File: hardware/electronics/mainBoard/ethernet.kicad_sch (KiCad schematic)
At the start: 29 parts, among them U4 LAN8742AI, U5 MRJ-5381-01

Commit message: fixed nets
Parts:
- removed C57: 1uF, symbol lib_sch:C
- removed C58, C59, C60: 100nF, symbol lib_sch:C
- removed C61: 10uF, symbol lib_sch:C
- removed C63: 100nF, symbol lib_sch:C_horizontal
- removed R31, R39: 33R, symbol lib_sch:R_horizontal
- removed R32: 10K, symbol lib_sch:R_horizontal
- removed R33, R34, R35, R36, R37, R47: 10K, symbol lib_sch:R
- removed R42, R43: 40R9, symbol lib_sch:R
- removed R45: 270R, symbol lib_sch:R
- added C47: 10uF, symbol lib_sch:C
- added C48, C49, C53: 100nF, symbol lib_sch:C
- added C50: 100nF, symbol lib_sch:C_horizontal
- added C52: 1uF, symbol lib_sch:C
- added R25, R26, R27: 41K2, symbol lib_sch:R
- added R28, R29, R30, R31, R32, R40: 10K, symbol lib_sch:R
- added R34, R36: 33R, symbol lib_sch:R_horizontal
- added R35: 10K, symbol lib_sch:R_horizontal
- C51: renamed from C56; DKPN (none) -> 478-12726-1-ND; MPN (none) -> 06035C471K4T4A; Manufacturer (none) -> KYOCERA AVX; Package PKG -> 0603; Tolerance TOL -> 10%; Voltage Rating VOLTAGE -> 50V
- L3: Current Rating IMAX -> 350mA; DC Resistance DCR -> 500mR; DKPN (none) -> 283-MFBA3V1608K-601-RCT-ND; MPN (none) -> MFBA3V1608K-601-R; Manufacturer (none) -> Eaton - Electronics Division; Package PKG -> 0603
- R24: renamed from R40; value 40R9 -> 41K2; DKPN (none) -> 541-41.2LCT-ND; MPN (none) -> CRCW040241R2FKED; Manufacturer (none) -> Vishay Dale; Package PKG -> 0402; Power Rating PWR -> 62m5W; Tolerance TOL -> 1%
- R33: renamed from R30; DKPN (none) -> 541-33.0LCT-ND; MPN (none) -> CRCW040233R0FKED; Manufacturer (none) -> Vishay Dale; Package PKG -> 0402; Power Rating PWR -> 62m5W; Tolerance TOL -> 1%
- R37: renamed from R44; DKPN (none) -> 541-12.1KLCT-ND; MPN (none) -> CRCW040212K1FKED; Manufacturer (none) -> Vishay Dale; Package PKG -> 0402; Power Rating PWR -> 62m5W; Tolerance TOL -> 1%
- R38: DKPN (none) -> 541-33.0LCT-ND; MPN (none) -> CRCW040233R0FKED; Manufacturer (none) -> Vishay Dale; Package PKG -> 0402; Power Rating PWR -> 62m5W; Tolerance TOL -> 1%
- R39: renamed from R46; DKPN (none) -> 541-270LCT-ND; MPN (none) -> CRCW0402270RFKED; Manufacturer (none) -> Vishay Dale; Package PKG -> 0402; Power Rating PWR -> 62m5W; Tolerance TOL -> 1%
- R41: value 40R9 -> 270R; DKPN (none) -> 541-270LCT-ND; MPN (none) -> CRCW0402270RFKED; Manufacturer (none) -> Vishay Dale; Package PKG -> 0402; Power Rating PWR -> 62m5W; Tolerance TOL -> 1%
- renumbered D4 to D2, U5 to U6, U4 to U7
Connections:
- net +3V3: now also C53.1, R28.1, R29.1, R30.1, R31.1, R32.1
- net 3V3_Ethernet: now also C47.1, C48.1, C49.1, C50.1, R25.1, R26.1, R27.1; no longer R41.1
- net CRS_DV: now also R30.2, R36.2; no longer R38.2
- net LED2: now also R40.1
- net REF_CLK: now also R38.2, R32.2
- net RMII.CRS_DV: now also R36.1; no longer R38.1
- net RMII.REF_CLK: now also R38.1
- net RXD0: now also R28.2
- net RXD1: now also R29.2, R34.2
- net RXER: now also R35.2
- net RXP: now also R25.2; no longer R41.2
- net TXN: now also R26.2
- net TXP: now also R27.2
- net VSS: now also R41.2, C47.2, C48.2, C49.2, C50.2, C52.2, C53.2, R35.1, R40.2
- net at U6.11 (LED(Green)_K): now also R41.1
- net at C51.1, U7.6 (VDDCR): now also C52.1
- net RMMI.MDC renamed RMII.MDC
- net RMMI.MDIO renamed RMII.MDIO
- net RMII.MDIO: now also R31.2
- net RMMI.RXD0 renamed RMII.RXD0
- net RMMI.TXD0 renamed RMII.TXD0
- net RMMI.TXD1 renamed RMII.TXD1
- net RMMI.TX_EN renamed RMII.TX_EN
- new net RMII.RXD1: R34.1
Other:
- moved on the sheet: D2, R39

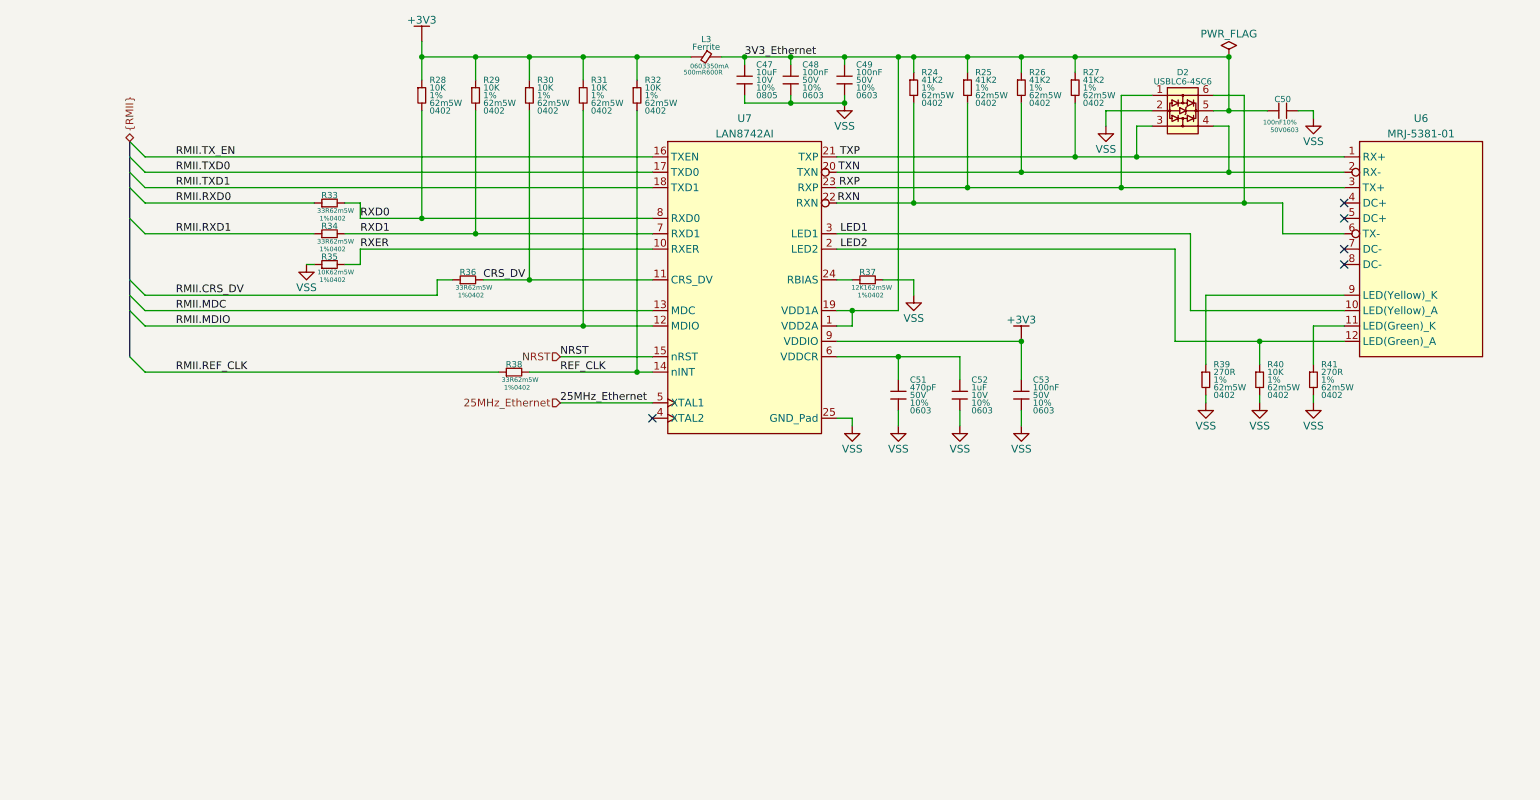
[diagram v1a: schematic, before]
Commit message: fixed net names and power flags
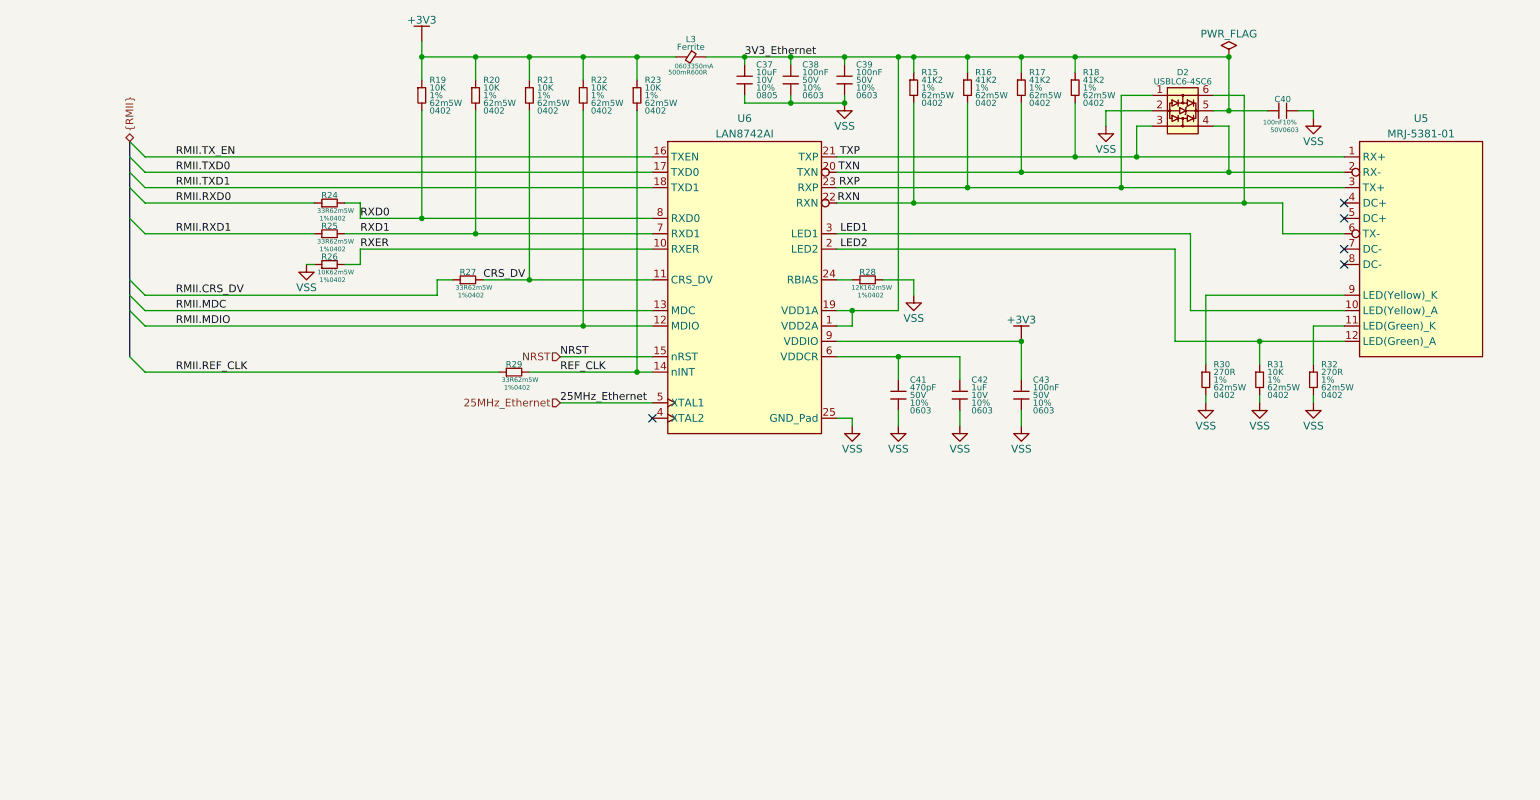
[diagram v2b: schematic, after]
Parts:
- renumbered C47 to C37, C48 to C38, C49 to C39, C50 to C40, C51 to C41, C52 to C42, C53 to C43, R24 to R15, R25 to R16, R26 to R17, R27 to R18, R28 to R19, R29 to R20, R30 to R21, R31 to R22, R32 to R23, R33 to R24, R34 to R25, R35 to R26, R36 to R27, R37 to R28, R38 to R29, R39 to R30, R40 to R31, R41 to R32, U6 to U5, U7 to U6
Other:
- moved on the sheet: L3

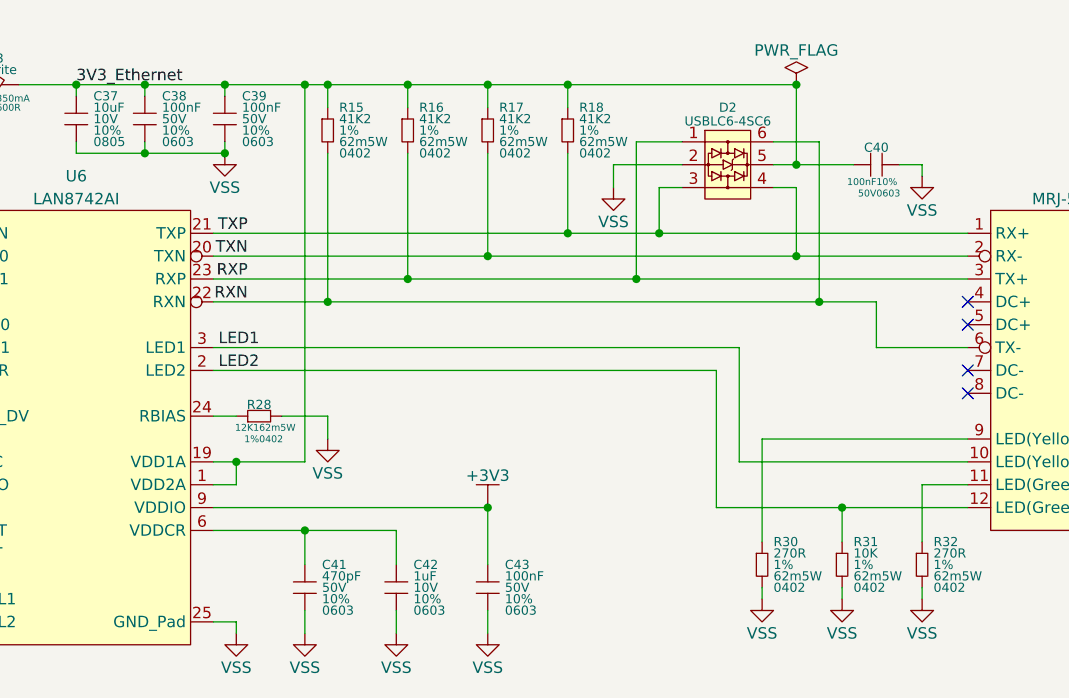
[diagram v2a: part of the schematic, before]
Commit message: updated capacitors
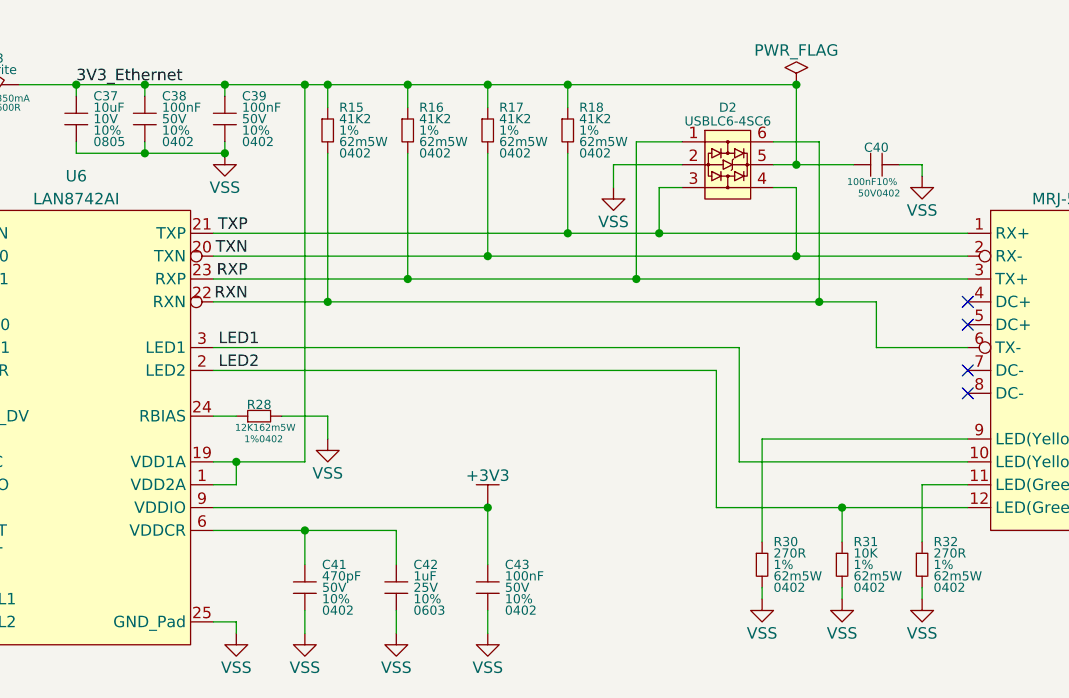
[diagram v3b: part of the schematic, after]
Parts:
- C37: DKPN 478-KAM21AR71A106KUCT-ND -> 490-10674-1-ND; MPN KAM21AR71A106KU -> GCM21BR71A106KE22L; Manufacturer KYOCERA AVX -> Murata Electronics
- C38, C39, C40, C43: DKPN 478-KAM15AR71H104KTCT-ND -> 490-GRT155R71H104KE01DCT-ND; MPN 06035C104K4T2A -> GRT155R71H104KE01D; Manufacturer KYOCERA AVX -> Murata Electronics; Package 0603 -> 0402
- C41: DKPN 478-12726-1-ND -> 490-GRT155R71H471KE01DCT-ND; MPN 06035C471K4T4A -> GRT155R71H471KE01D; Manufacturer KYOCERA AVX -> Murata Electronics; Package 0603 -> 0402
- C42: DKPN 478-KAM15AR71A105KTCT-ND -> 490-GRT188R71E105KE13DCT-ND; MPN KAM15AR71A105KT -> GRT188R71E105KE13D; Manufacturer KYOCERA AVX -> Murata Electronics; Voltage Rating 10V -> 25V

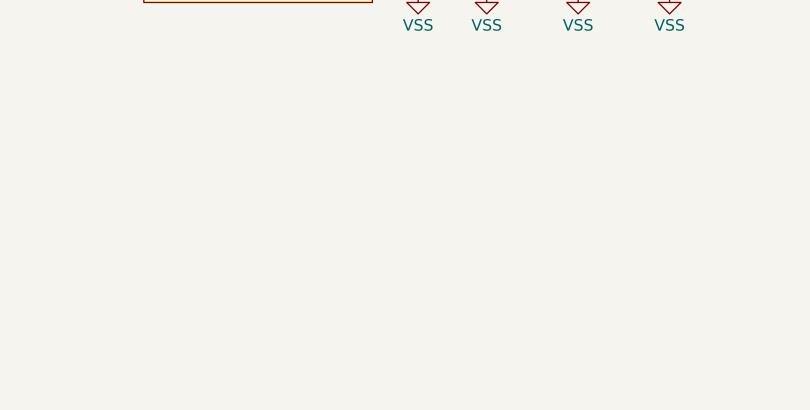
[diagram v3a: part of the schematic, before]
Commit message: added testpoints
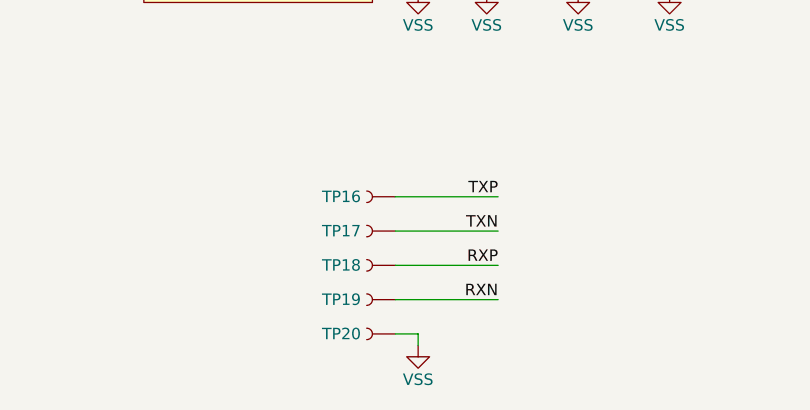
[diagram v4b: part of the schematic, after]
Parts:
- added TP16, TP17, TP18, TP19: ~, symbol lib_sch:Testpoint
- added TP20: RCWCTE, symbol lib_sch:Testpoint
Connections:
- net RXN: now also TP19.1
- net RXP: now also TP18.1
- net TXN: now also TP17.1
- net TXP: now also TP16.1
- net VSS: now also TP20.1

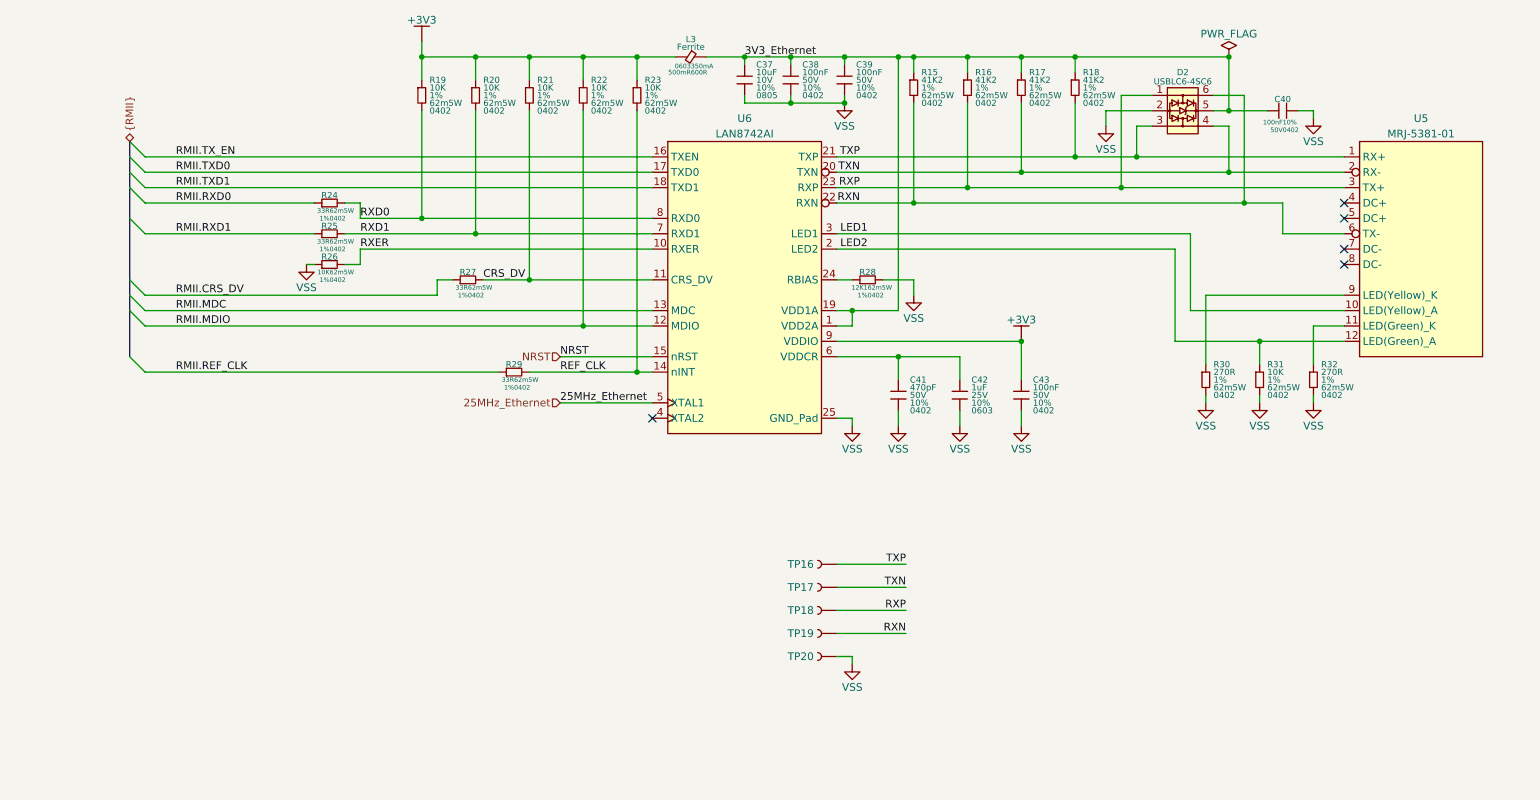
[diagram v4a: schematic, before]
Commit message: updated symbol refs
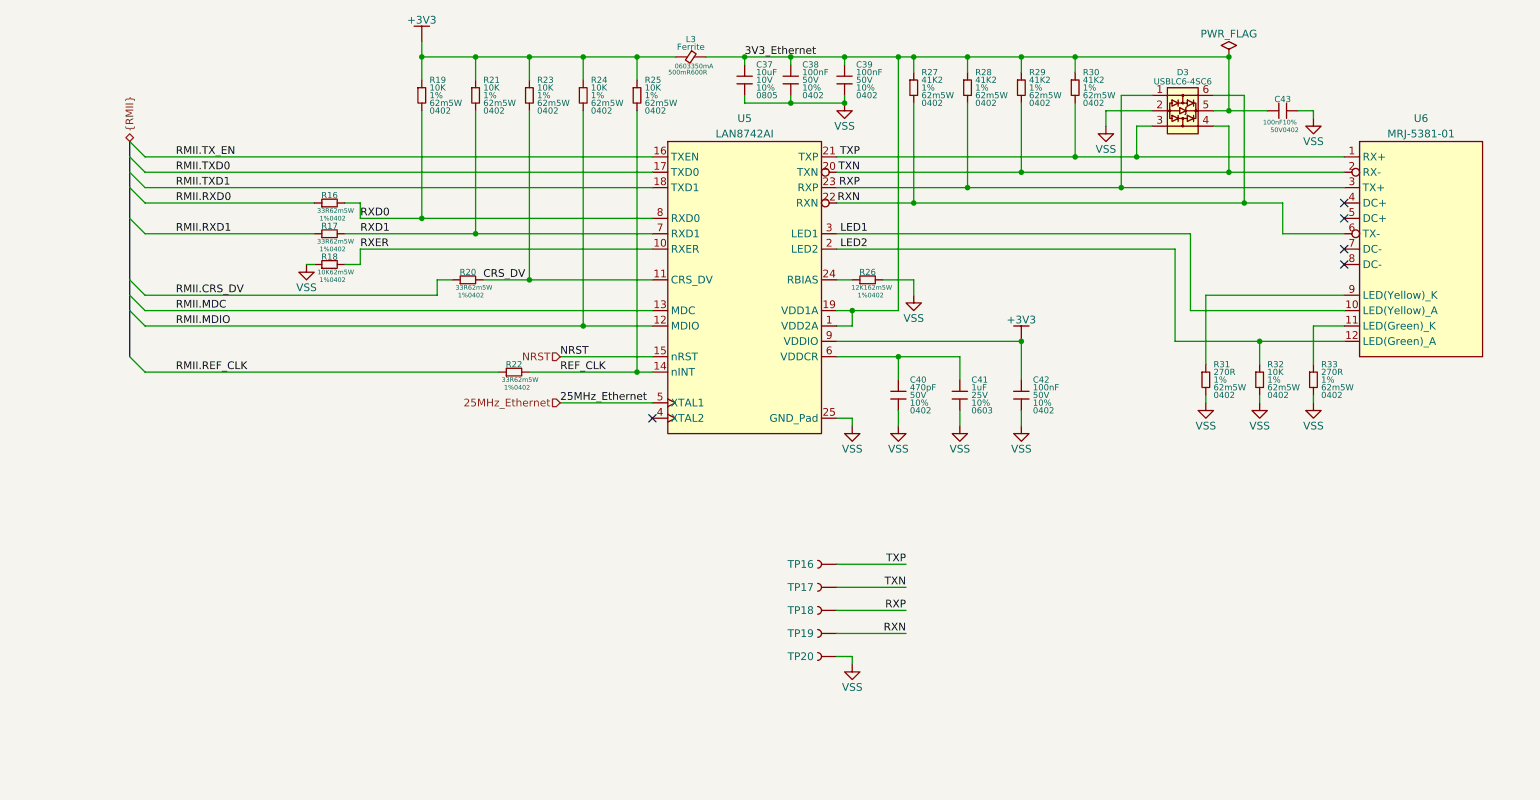
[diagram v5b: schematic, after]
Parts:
- renumbered C41 to C40, C42 to C41, C43 to C42, C40 to C43, D2 to D3, R24 to R16, R25 to R17, R26 to R18, R27 to R20, R20 to R21, R29 to R22, R21 to R23, R22 to R24, R23 to R25, R28 to R26, R15 to R27, R16 to R28, R17 to R29, R18 to R30, R30 to R31, R31 to R32, R32 to R33, U6 to U5, U5 to U6

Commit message: updated symbol refs
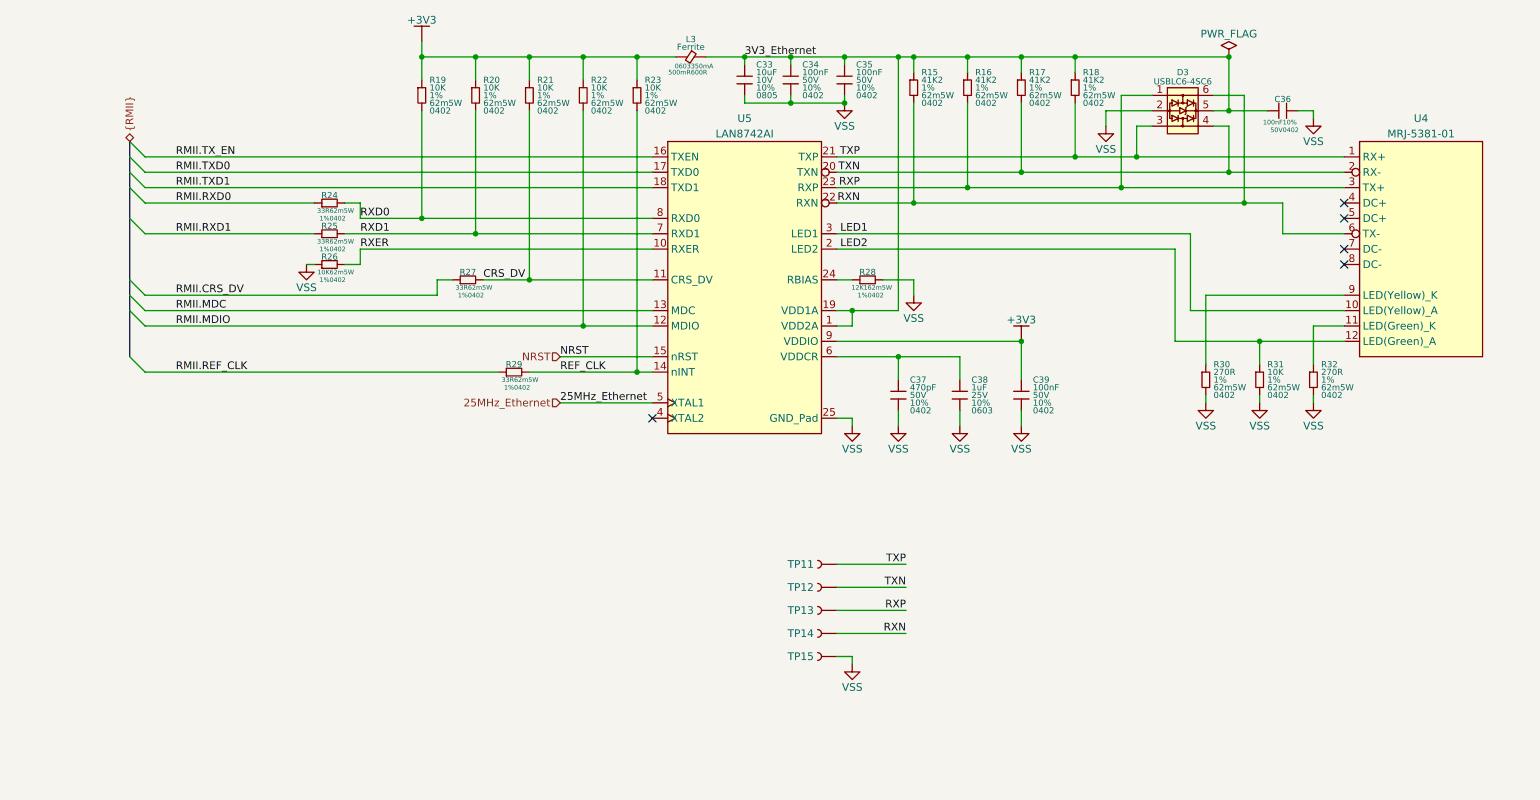
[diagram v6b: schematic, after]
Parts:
- renumbered C37 to C33, C38 to C34, C39 to C35, C43 to C36, C40 to C37, C41 to C38, C42 to C39, R27 to R15, R28 to R16, R29 to R17, R30 to R18, R21 to R20, R23 to R21, R24 to R22, R25 to R23, R16 to R24, R17 to R25, R18 to R26, R20 to R27, R26 to R28, R22 to R29, R31 to R30, R32 to R31, R33 to R32, TP16 to TP11, TP17 to TP12, TP18 to TP13, TP19 to TP14, TP20 to TP15, U6 to U4

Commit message: assigned FPs
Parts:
- D3: footprint (none) -> lib_ICs:SOT2395P280X145-6
- U4: footprint (none) -> lib_connectors:MJR-5381-X1
- U5: footprint (none) -> lib_ICs:QFN50P400X400X90-24
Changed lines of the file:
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@@
 			)
 		)
-		(property "Footprint" ""
+		(property "Footprint" "lib_connectors:MJR-5381-X1"
 			(at 251.46 107.95 0)
 			(effects
@@
 			)
 		)
-		(property "Footprint" ""
+		(property "Footprint" "lib_ICs:SOT2395P280X145-6"
 			(at 212.09 85.09 0)
 			(effects
@@
 			)
 		)
-		(property "Footprint" ""
+		(property "Footprint" "lib_ICs:QFN50P400X400X90-24"
 			(at 139.7 114.3 0)
 			(effects
